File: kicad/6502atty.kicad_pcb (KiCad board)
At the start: 2 copper layers, 100 x 101.6 mm, 104 parts, among them J1 Conn_01x04_Pin, J10 Conn_01x04_Pin, J11 Conn_01x03_Pin, J12 Conn_01x02_Pin, J2 Conn_01x02_Pin, J3 Conn_02x03_Odd_Even, J4 Conn_01x03_Pin, J5 Conn_01x06_Pin, J6 Conn_01x04_Pin, J7 Conn_01x10_Pin, J9 Conn_01x10_Pin, SW1 SW_Push, U1 ATmega164P-20P, U10 74LS08, U11 74LS138, U12 74LS574, U2 74LS112, U3 W65C02SxP, U4 74LS574, U5 74HC245, U6 27C128, U7 KM62256CLP, U8 74LS00, U9 74LS00, Y1 18.432MHz

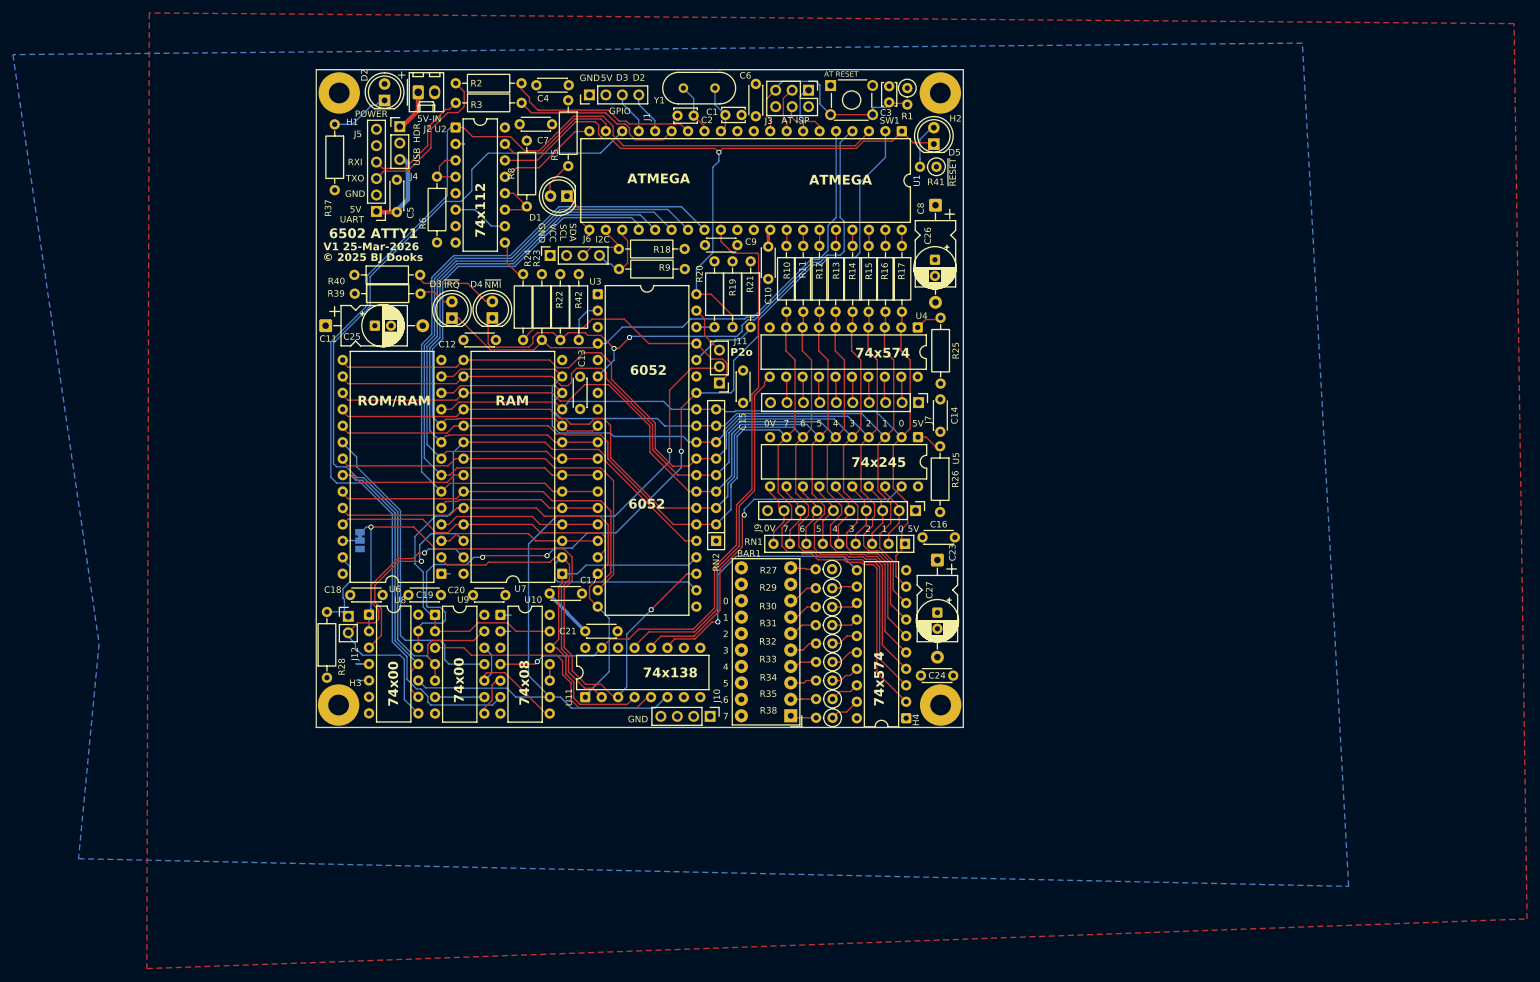
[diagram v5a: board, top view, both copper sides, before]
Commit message: kicad: routing and board updates
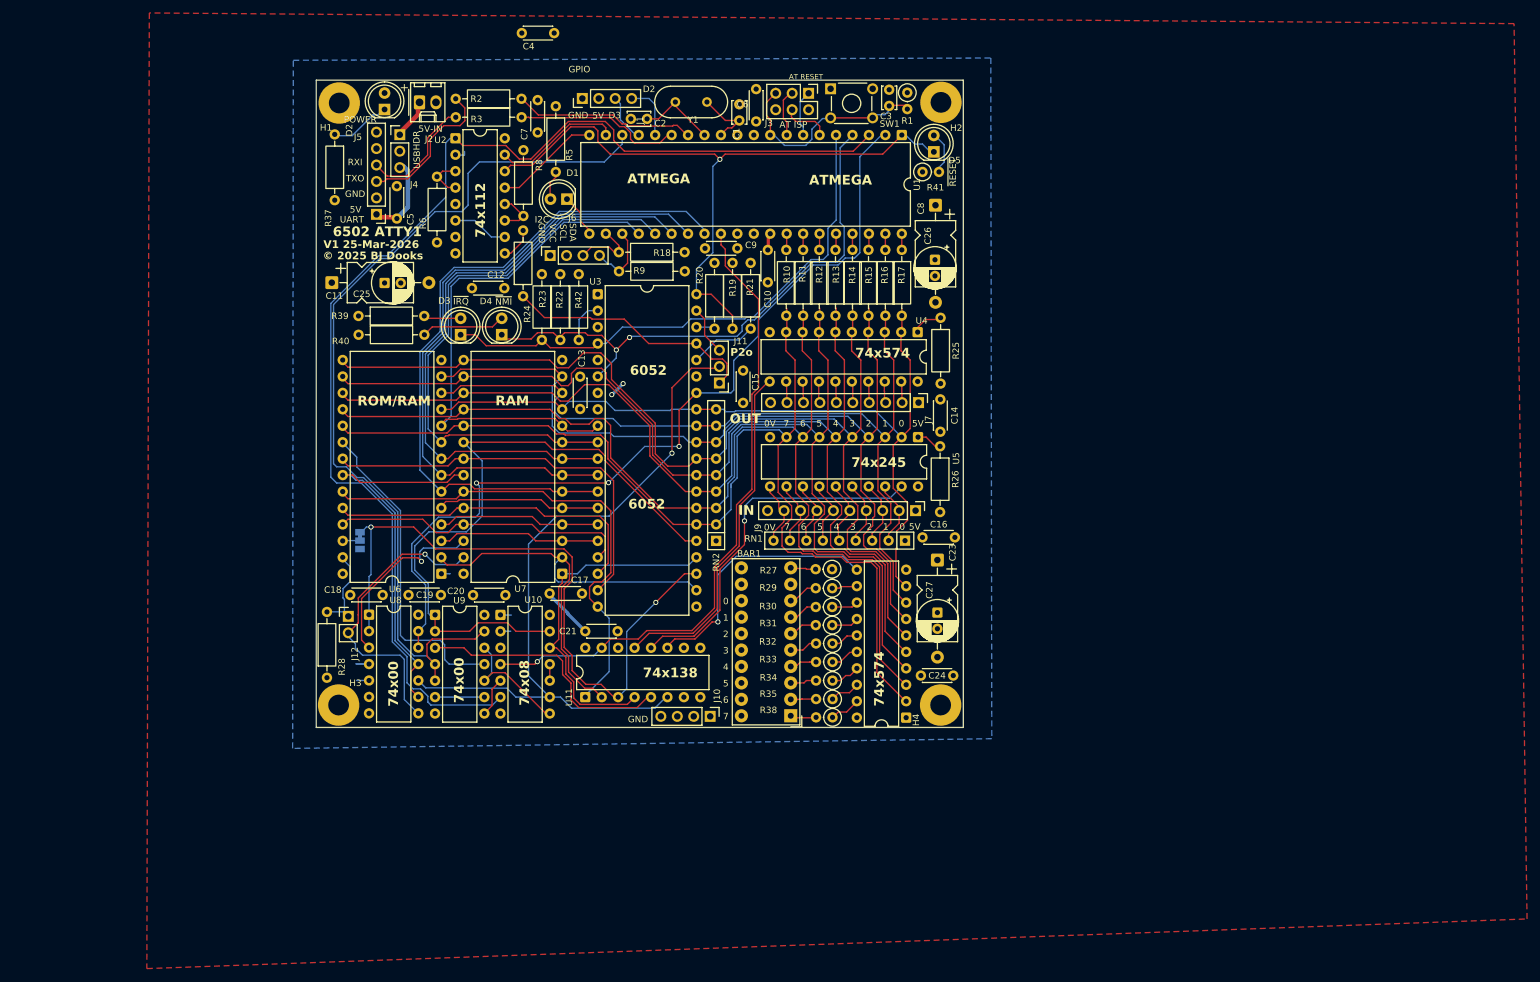
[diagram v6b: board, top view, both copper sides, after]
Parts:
- moved C12 10.2 mm to (29.1, 33.8), turned to 180 degrees
- moved R40 9.27 mm to (6.59, 41.0)
- moved C4 8.36 mm to (36.8, -5.65)
- moved C2 7.22 mm to (51.1, 7.60)
- moved C25 6.77 mm to (10.6, 33.0)
- moved R24 6.75 mm to (32.0, 35.0)
- moved C11 6.72 mm to (2.45, 32.9)
- moved R39 3.50 mm to (6.57, 38.0)
- moved C7 3.05 mm to (34.2, 9.70), turned to 90 degrees
- moved D4 2.98 mm to (28.7, 41.0)
- moved D3 2.91 mm to (22.4, 41.0)
- moved Y1 2.48 mm to (60.4, 5.00)
- moved R2 2.40 mm to (31.8, 4.50)
- moved C1 2.31 mm to (65.4, 7.85), turned to 90 degrees
- moved R41 2.29 mm to (93.7, 15.8), turned to 0 degrees
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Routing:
- net /CPU_~{NMI}: track 95.4 -> 87.9 mm
- net /Atmel Controller/AT_XTI: track 8.03 -> 13.0 mm
- net /A15: track 97.0 -> 101.8 mm
- net /CPU_~{IRQ}: track 87.3 -> 83.9 mm
- net /A0: track 85.1 -> 82.0 mm
- net /AT_~{CE}: track 102.5 -> 99.7 mm
- net /ROM_SEL: track 137.1 -> 139.7 mm
- net VCC: track 8.35 -> 10.8 mm, vias 0 -> 2
- net /Atmel Controller/AT_XTO: track 7.60 -> 9.99 mm
- net /R~{W}: track 134.8 -> 137.2 mm
- net /R~{W}ph: track 49.2 -> 47.0 mm
- net /Atmel Controller/PD2: track 6.87 -> 8.72 mm
- net /A2: track 96.2 -> 94.7 mm
- net Net-(U2B-J): track 8.30 -> 6.81 mm
- net Net-(U2B-Q): track 6.66 -> 5.24 mm
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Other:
- board size 100 x 101.6 mm -> 100 x 100 mm
- board text added: "IN"
- board text added: "OUT"
